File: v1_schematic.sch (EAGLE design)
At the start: 41 parts, among them IC2 FT232RL, IC3 SP3223EBP, Q1 25MHz, Q2 32.768kHz, X1 MINI-USB-32005-201

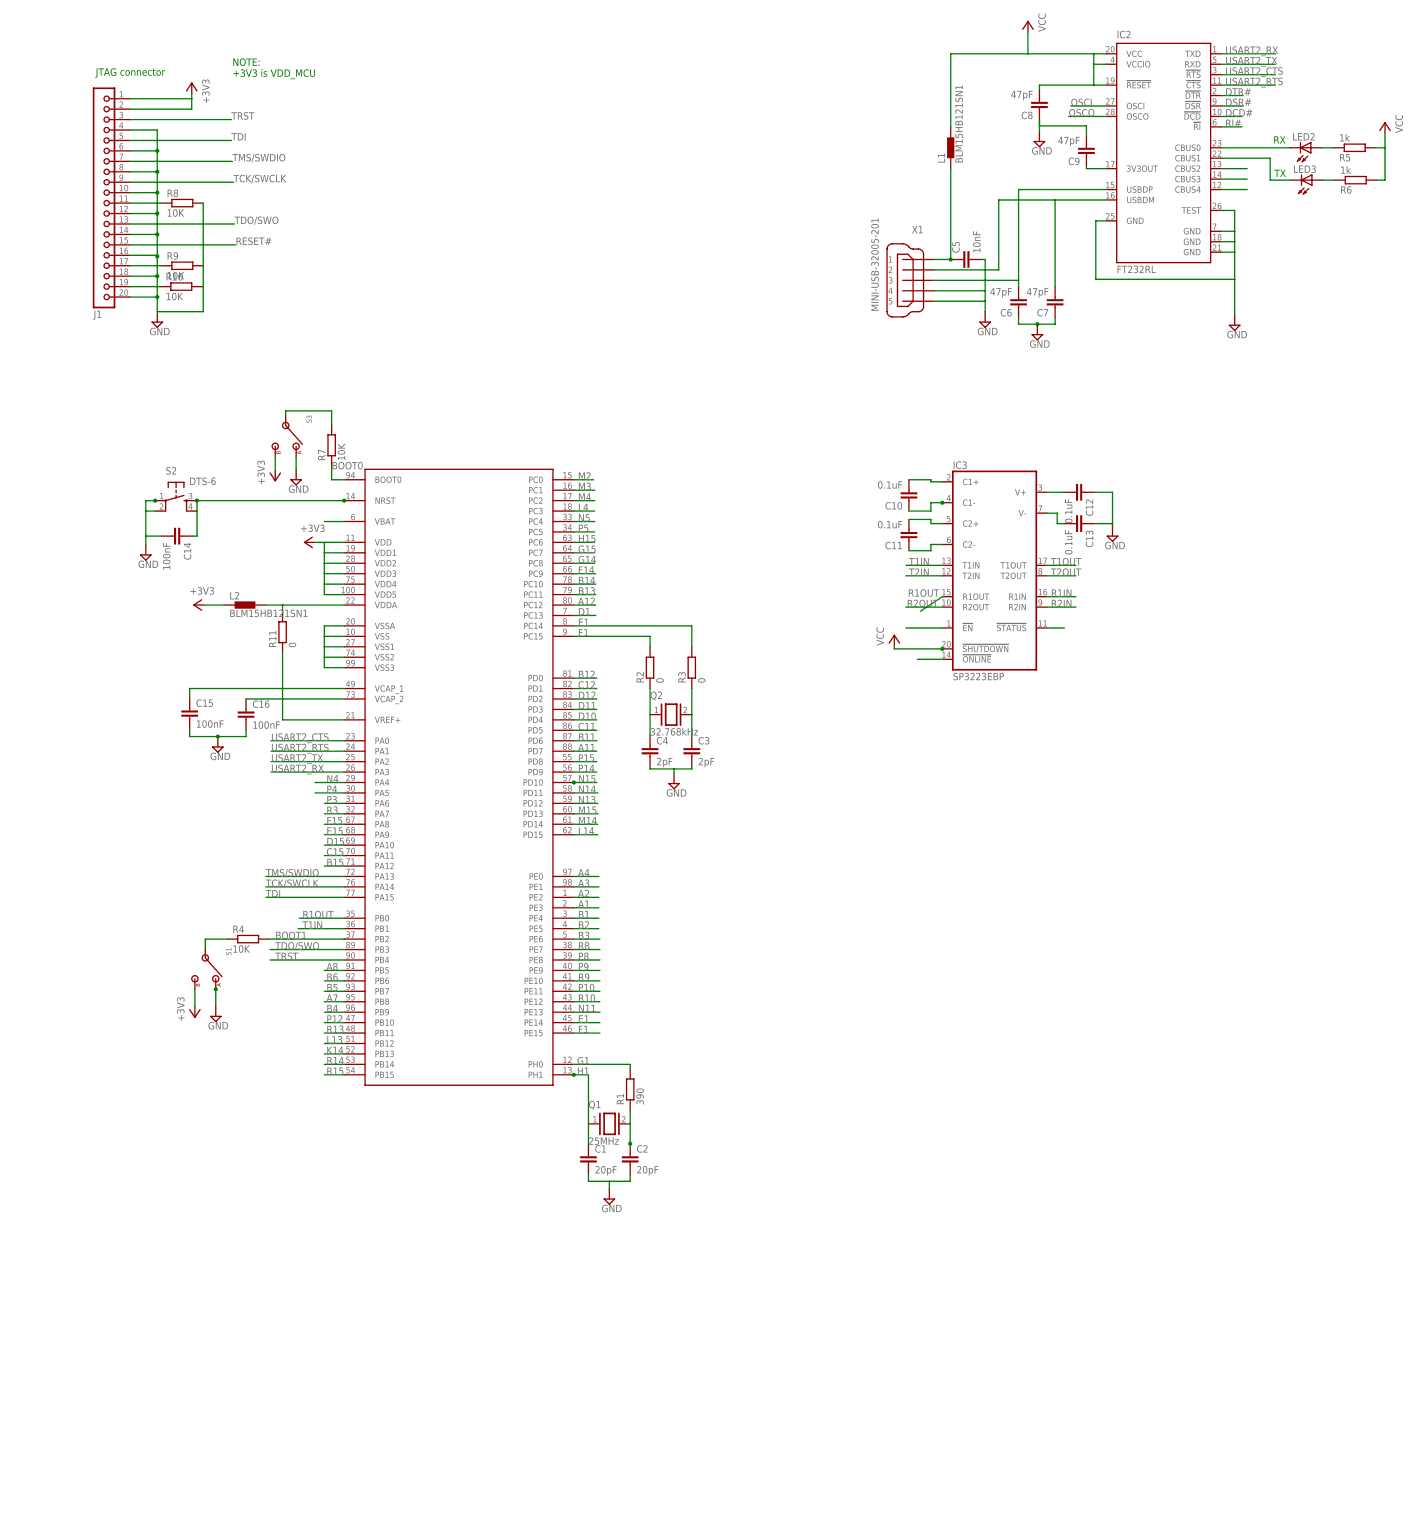
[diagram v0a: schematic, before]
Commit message: Decoupling and fixes
- Added decoupling capacitor network to MCU
- Fixes: conventions for component arrangement and enlargement of frame size
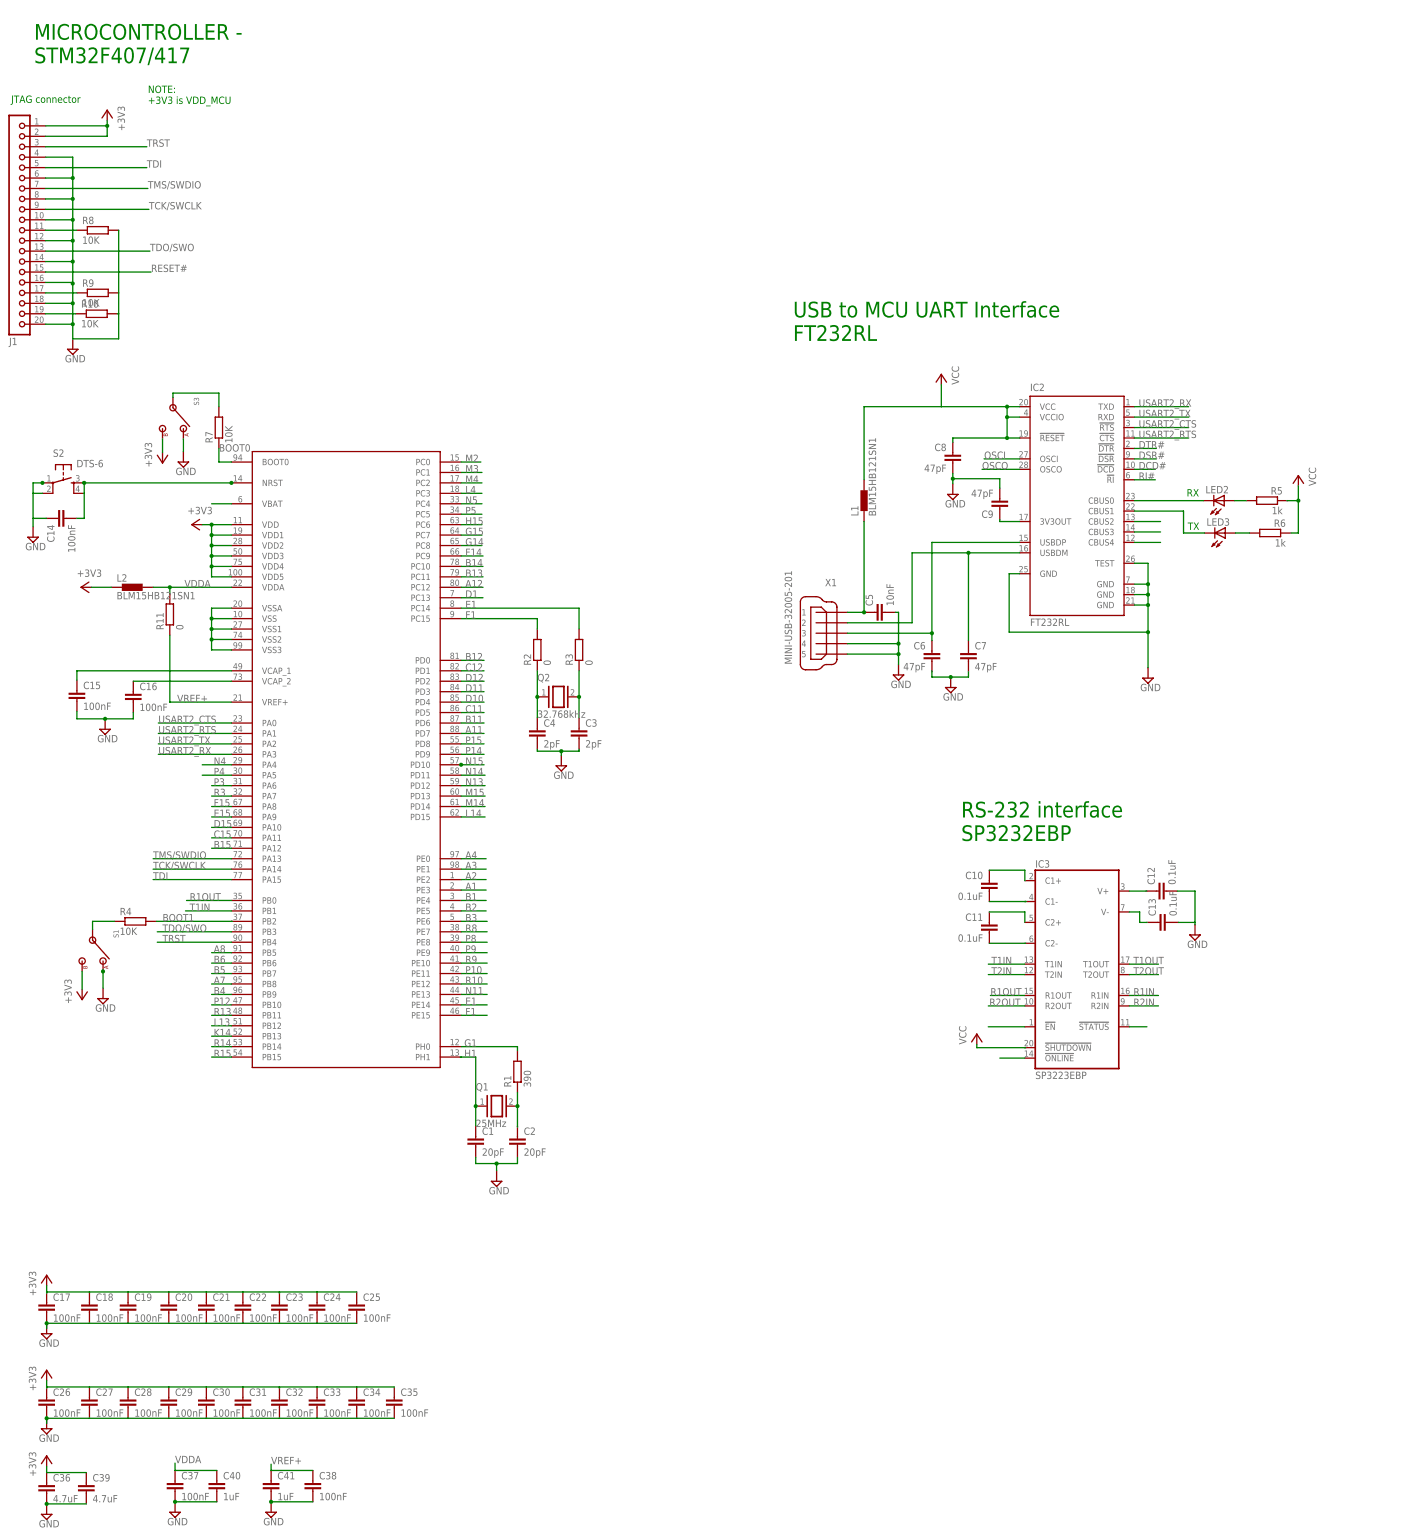
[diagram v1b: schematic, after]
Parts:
- added C17, C18, C19, C20, C21, C22, C23, C24, C25, C26, C27, C28, C29, C30, C31, C32, C33, C34, C35, C37, C38: 100nF, resistor:C-EUC0805
- added C36, C39: 4.7uF, resistor:C-EUC0805
- added C40, C41: 1uF, resistor:C-EUC0805
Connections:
- removed net N$33: L2.2, R11.2, U$1.VDDA
- removed net N$41: R11.1, U$1.VREF+
- new net VDDA: C37.1, C40.1, L2.2, R11.2, U$1.VDDA
- new net VREF+: C38.1, C41.1, R11.1, U$1.VREF+
- net +3V3: now also C18.1, C19.1, C20.1, C21.1, C22.1, C24.1, C25.1, C27.1, C28.1, C29.1, C30.1, C31.1, C33.1, C34.1, C35.1, C36.1, C39.1
- net GND: now also C12.2, C13.2, C17.2, C18.2, C19.2, C20.2, C21.2, C22.2, C23.2, C24.2, C25.2, C26.2, C27.2, C28.2, C29.2, C30.2, C31.2, C32.2, C33.2, C34.2, C35.2, C36.2, C37.2, C38.2, C39.2, C40.2, C41.2, C7.2, C8.2; no longer C12.1, C13.1, C14.2, C6.1, C7.1, C8.1
- net N$12: now also C7.1; no longer C7.2
- net N$13: now also C6.1; no longer C6.2
- net N$16: now also LED3.A, R6.2; no longer LED2.A, R5.1
- net N$17: now also LED2.A, R5.2; no longer LED3.A, R6.1
- net N$18: now also IC3G$1.C1-; no longer IC3G$1.C1+
- net N$19: now also C11.2; no longer C10.1, IC3G$1.C1-
- net N$20: now also C11.1; no longer C11.2
- net N$21: now also C10.1, IC3G$1.C1+; no longer C11.1, IC3G$1.C2-
- net N$22: no longer C12.2
- net N$23: now also C13.1; no longer C13.2
- net N$24: now also C14.2; no longer C14.1
- net VCC: now also C8.1, R6.1; no longer C8.2, R5.2, R6.2
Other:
- note added: "MICROCONTROLLER - STM32F407/417"
- note added: "RS-232 interface SP3232EBP"
- note added: "USB to MCU UART Interface FT232RL"
- moved on the sheet: C1, C10, C11, C12, C13, C14, C15, C16, C2, C3, C4, C5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

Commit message: Updates and fixes
- completed RS232 interfacing, added DB9 connector
- added CAN contoller interface with DB9 connector
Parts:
- added C42: 0.1uF, resistor:C-EUC0805
- added IC1: PCA82C250, micro-philips:PCA82C250
- added R12: 25K to 200K, pot-vitrohm:PC25
- added R13, R14: 120, resistor:R-EU_R0805
- added X2, X3: (no value), con-subd:F09VB
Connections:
- net B15 renamed CAN1_TX
- net C15 renamed CAN1_RX
- net L13 renamed USART3_CK
- removed net K14: U$1.PB13
- removed net N$22 (its old number): IC3G$1.V+
- removed net P12: U$1.PB10
- removed net R13: U$1.PB11
- removed net R14: U$1.PB14
- removed net USART2_CTS: IC2.!RTS, U$1.PA0
- removed net USART2_RTS: IC2.!CTS, U$1.PA1
- new net CANH: R13.2, R14.2, X3.7
- new net CANL: R13.1, R14.1, X3.2
- new net N$23: C12.1, IC3G$1.V+
- new net N$28: R12.E
- new net UART4_RX: IC3G$1.R1OUT, U$1.PA1
- new net UART4_TX: IC3G$1.T1IN, U$1.PA0
- new net USART3_CTS: IC2.!RTS, U$1.PB13
- new net USART3_RTS: IC2.!CTS, U$1.PB14
- new net USART3_RX: IC2.TXD, U$1.PB11
- new net USART3_TX: IC2.RXD, U$1.PB10
- net GND: now also C42.2, IC1.GND, R12.A, X2.5, X3.3
- net R1IN: now also X2.2
- net R1OUT: no longer IC3G$1.R1OUT
- net T1IN: no longer IC3G$1.T1IN
- net T1OUT: now also X2.3
- net USART2_RX: no longer IC2.TXD
- net USART2_TX: no longer IC2.RXD
- net VCC: now also C42.1, IC1.VCC
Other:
- note added: "CAN CONTROLLER INTERFACE"
- note added: "POWER DECOUPLING CAPACITORS"
- moved on the sheet: C12, C13

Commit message: RS-485 Interface
- added the rs-485 interface to MCU
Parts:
- added IC4: MAX481CPA, maxim:MAX481CPA
- added T1: ST02-3.5MM, con-dinkle:ST02-3.5MM
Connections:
- net B5 renamed USART1_RX
- net B6 renamed USART1_TX
- net D11 renamed USART2_CTS
- removed net B11: U$1.PD6
- removed net C11: U$1.PD5
- removed net D10: U$1.PD4
- new net N$27: IC4G$1.B, T1.1
- new net N$29: IC4G$1.A, T1.2
- new net USART2_RTS: IC4G$1.DE, IC4G$1.RE/, U$1.PD4
- net CAN1_RX: now also IC1.TXD
- net CAN1_TX: now also IC1.RXD
- net CANH: now also IC1.CANH
- net N$19: now also IC3G$1.C2-
- net N$28: now also IC1.RS
- net USART2_RX: now also IC4G$1.RO, U$1.PD6
- net USART2_TX: now also IC4G$1.DI, U$1.PD5
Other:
- note added: "CAN CONTROLLER INTERFACE PCA8C250"
- note added: "RS-485 Interface MAX481CPA"
- note removed: "CAN CONTROLLER INTERFACE"
- moved on the sheet: C10, C11, C12, C13, C3, C4, C42, IC1, IC3, Q2, R12, R13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
